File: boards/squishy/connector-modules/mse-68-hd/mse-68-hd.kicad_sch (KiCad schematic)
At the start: 14 parts, among them J1 SCSI PHY Mezz, J3 Conn_01x04, J4 Conn_02x34_Clockwise_Shield, U1 M24C02-RMC

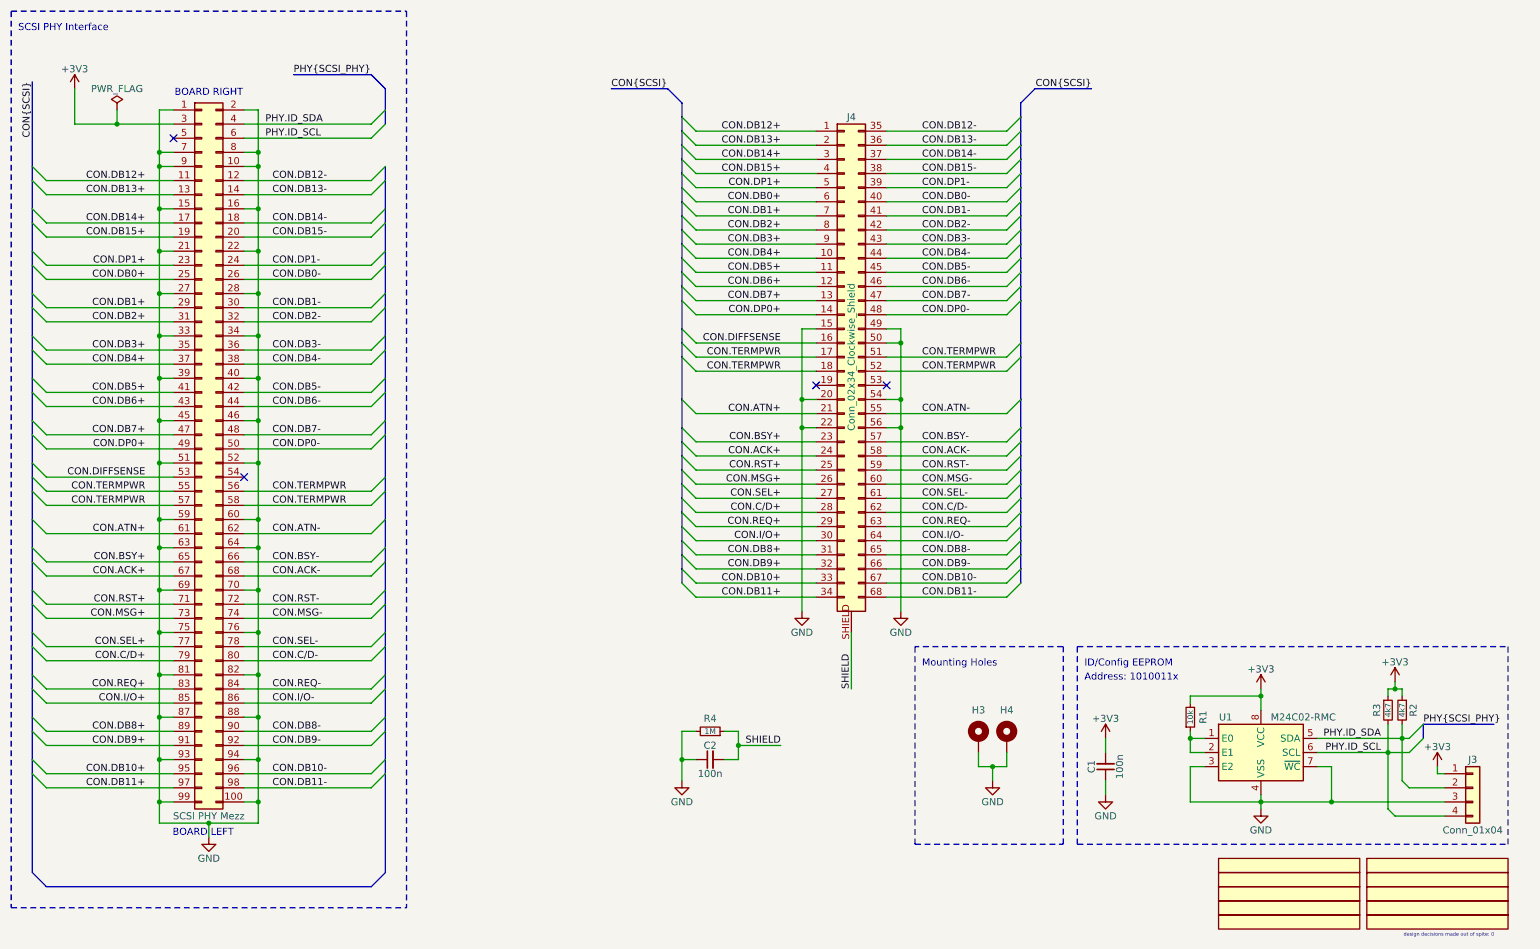
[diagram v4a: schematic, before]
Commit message: squishy: connectors: Cleaned up and unified look/feel of connector schematics
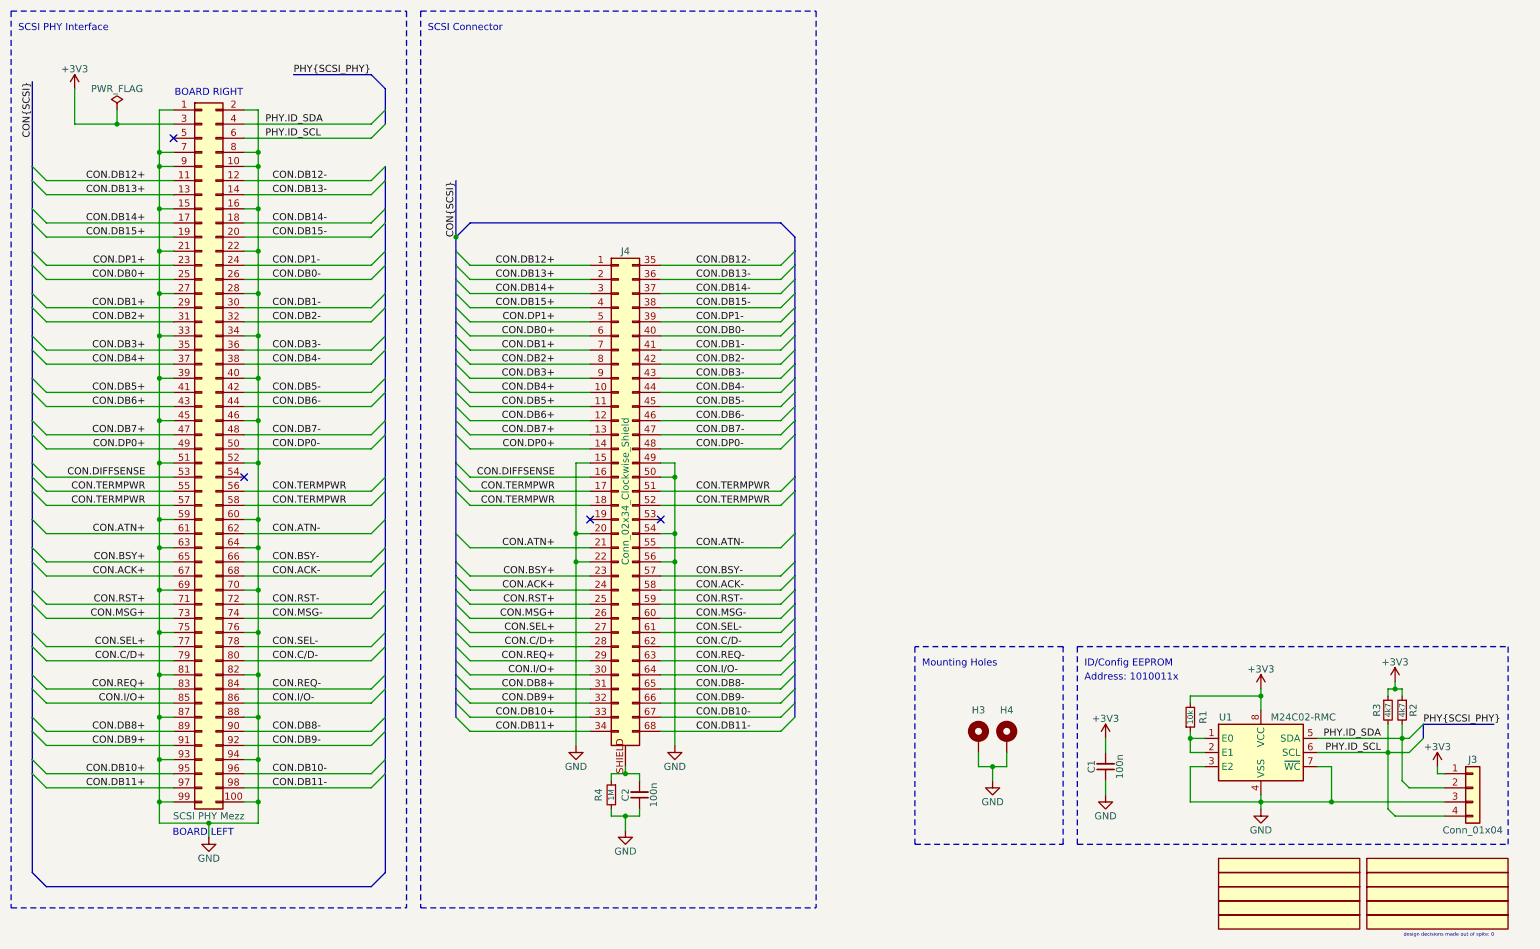
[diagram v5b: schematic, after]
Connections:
- net SHIELD: no longer names the net of C2.2, J4.SHIELD, R4.1
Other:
- note added: "SCSI Connector"
- moved on the sheet: C2, J4, R4

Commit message: squishy: connectors: updated schematic title blocks for connectors as appropriate
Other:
- title: Squishy -  ICD 50 -> Squishy -  SCSI LVD/MSE/SE HD 68 Connector Module
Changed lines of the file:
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@@
 	(paper "A4")
 	(title_block
-		(title "Squishy -  ICD 50")
-		(date "2024-08-22")
+		(title "Squishy -  SCSI LVD/MSE/SE HD 68 Connector Module")
+		(date "2024-09-17")
 		(rev "1")
 		(company "Shrine Maiden Heavy Industries")
